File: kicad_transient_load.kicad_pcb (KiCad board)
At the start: 2 copper layers, 8 parts, among them J1 BNC In, J2 Screw_Terminal_01x02, J3 Conn_02x03_Odd_Even, Q1 ZVN4306A

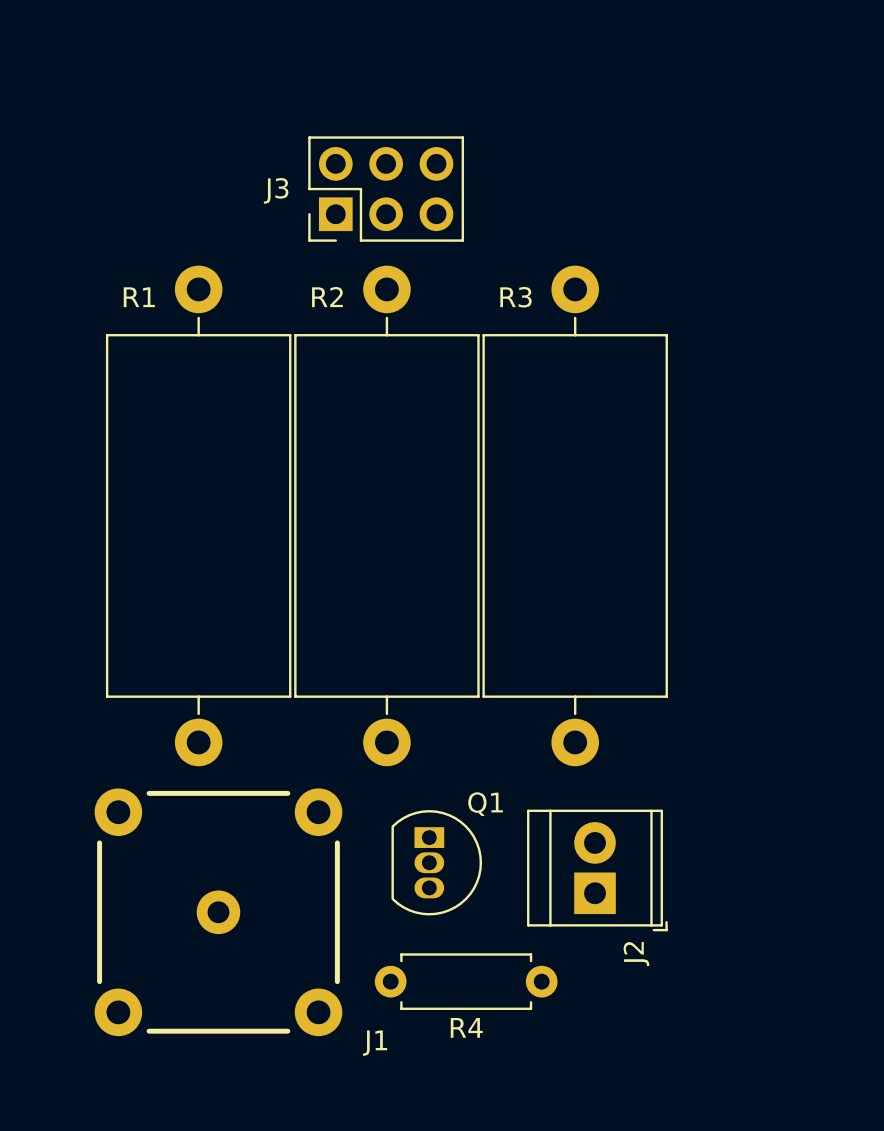
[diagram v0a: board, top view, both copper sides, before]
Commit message: route all but gnd plane, add screw holes and board outline
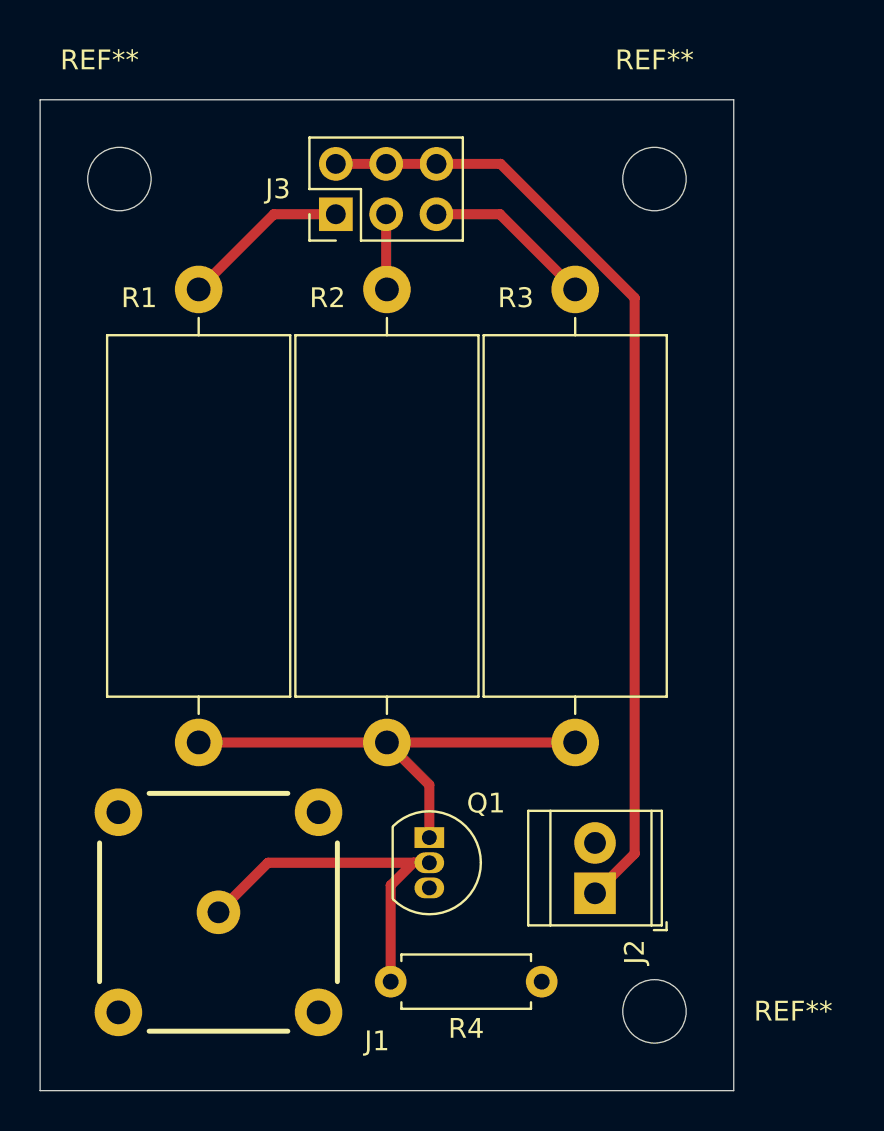
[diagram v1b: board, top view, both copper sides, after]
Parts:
- added REF**: MountingHole_3.2mm_M3, MountingHole:MountingHole_3.2mm_M3, F.Cu at (146.0, 59.0)
- added REF**: MountingHole_3.2mm_M3, MountingHole:MountingHole_3.2mm_M3, F.Cu at (119.0, 59.0)
- added REF**: MountingHole_3.2mm_M3, MountingHole:MountingHole_3.2mm_M3, F.Cu at (146.0, 101.0)
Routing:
- net /power supply in: track 0.00 -> 48.8 mm
- net Net-(Q1-D): track 0.00 -> 24.7 mm
- net /bnc_in: track 0.00 -> 19.0 mm
- net Net-(J3-Pin_5): track 0.00 -> 8.57 mm
- net Net-(J3-Pin_1): track 0.00 -> 8.49 mm
- net Net-(J3-Pin_3): track 0.00 -> 3.81 mm
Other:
- board outline added: 35 x 50 mm

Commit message: finished pcb
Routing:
- added copper zone on B.Cu, net GND
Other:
- board text added: "HugonLabs"
- board text added: "Transient Load v1.0 2024-04-05"
- board text added: "Transient Load v1.0 2024-04-05 HugonLabs"
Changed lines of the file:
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@@
 		(title "Transient Load")
 		(date "2024-04-05")
+		(rev "v1.0")
 		(company "HugonLabs")
 		(comment 1 "For performing transient analysis of power supplies")
@@
 		(layer "Edge.Cuts")
 	)
+	(gr_text "Transient Load v1.0\n2024-04-05\nHugonLabs"
+		(at 139 78 0)
+		(layer "B.SilkS")
+		(effects
+			(font
+				(size 1 1)
+				(thickness 0.15)
+			)
+			(justify left bottom mirror)
+		)
+	)
+	(gr_text "Transient Load v1.0 2024-04-05"
+		(at 149 93 90)
+		(layer "F.SilkS")
+		(effects
+			(font
+				(size 1 1)
+				(thickness 0.15)
+			)
+			(justify left bottom)
+		)
+	)
+	(gr_text "HugonLabs"
+		(at 117 81.5 90)
+		(layer "F.SilkS")
+		(effects
+			(font
+				(size 1 1)
+				(thickness 0.15)
+			)
+			(justify left bottom)
+		)
+	)
 	(segment
 		(start 134.64 93.5)
@@
 		(net 7)
 	)
+	(zone
+		(net 1)
+		(net_name "GND")
+		(layer "B.Cu")
+		(name "gnd_plane")
+		(hatch edge 0.5)
+		(connect_pads
+			(clearance 0.5)
+		)
+		(min_thickness 0.25)
+		(filled_areas_thickness no)
+		(fill yes
+			(thermal_gap 0.5)
+			(thermal_bridge_width 0.5)
+			(smoothing fillet)
+			(radius 2)
+		)
+		(polygon
+			(pts
+				(xy 116.5 103.5) (xy 116.5 63) (xy 123 63) (xy 127.5 56) (xy 137.5 56) (xy 144.5 63) (xy 148 63)
+				(xy 148 97) (xy 143 97) (xy 141 103.5)
+			)
+		)
+	)
 )
